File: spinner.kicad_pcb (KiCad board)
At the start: 2 copper layers, 39 parts, among them SW1 SW_SPDT, U1 SFH617A-3X006, U2 SFH617A-3X006, U3 SFH617A-3X006, U4 RS0102, U5 AP63205WU

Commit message: IDK.  Add the kitchen sink.
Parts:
- added C109: .1uF, Capacitor_SMD:C_0805_2012Metric_Pad1.18x1.45mm_HandSolder, B.Cu at (145.0, 154.0)
- added C110: .1uF, Capacitor_SMD:C_0805_2012Metric_Pad1.18x1.45mm_HandSolder, B.Cu at (145.0, 160.0)
- added C111: .1uF, Capacitor_SMD:C_0805_2012Metric_Pad1.18x1.45mm_HandSolder, B.Cu at (145.0, 166.0)
- added C112: .1uF, Capacitor_SMD:C_0805_2012Metric_Pad1.18x1.45mm_HandSolder, B.Cu at (145.0, 172.0)
- added C113: .1uF, Capacitor_SMD:C_0805_2012Metric_Pad1.18x1.45mm_HandSolder, B.Cu at (145.0, 178.0)
- added C114: .1uF, Capacitor_SMD:C_0805_2012Metric_Pad1.18x1.45mm_HandSolder, B.Cu at (145.0, 184.0)
- added C115: .1uF, Capacitor_SMD:C_0805_2012Metric_Pad1.18x1.45mm_HandSolder, B.Cu at (145.0, 190.0)
- added C201: .1uF, Capacitor_SMD:C_0805_2012Metric_Pad1.18x1.45mm_HandSolder, B.Cu at (157.7, 101.3)
- added C202: .1uF, Capacitor_SMD:C_0805_2012Metric_Pad1.18x1.45mm_HandSolder, B.Cu at (162.9, 98.3)
- added C203: .1uF, Capacitor_SMD:C_0805_2012Metric_Pad1.18x1.45mm_HandSolder, B.Cu at (168.1, 95.3)
- added C204: .1uF, Capacitor_SMD:C_0805_2012Metric_Pad1.18x1.45mm_HandSolder, B.Cu at (173.3, 92.3)
- added C205: .1uF, Capacitor_SMD:C_0805_2012Metric_Pad1.18x1.45mm_HandSolder, B.Cu at (178.5, 89.3)
- added C206: .1uF, Capacitor_SMD:C_0805_2012Metric_Pad1.18x1.45mm_HandSolder, B.Cu at (183.7, 86.3)
- added C207: .1uF, Capacitor_SMD:C_0805_2012Metric_Pad1.18x1.45mm_HandSolder, B.Cu at (188.9, 83.3)
- added C208: .1uF, Capacitor_SMD:C_0805_2012Metric_Pad1.18x1.45mm_HandSolder, B.Cu at (194.1, 80.3)
- added C209: .1uF, Capacitor_SMD:C_0805_2012Metric_Pad1.18x1.45mm_HandSolder, B.Cu at (199.3, 77.3)
- added C210: .1uF, Capacitor_SMD:C_0805_2012Metric_Pad1.18x1.45mm_HandSolder, B.Cu at (204.5, 74.3)
- added C211: .1uF, Capacitor_SMD:C_0805_2012Metric_Pad1.18x1.45mm_HandSolder, B.Cu at (209.7, 71.3)
- added C212: .1uF, Capacitor_SMD:C_0805_2012Metric_Pad1.18x1.45mm_HandSolder, B.Cu at (214.9, 68.3)
- added C213: .1uF, Capacitor_SMD:C_0805_2012Metric_Pad1.18x1.45mm_HandSolder, B.Cu at (220.0, 65.3)
- added C214: .1uF, Capacitor_SMD:C_0805_2012Metric_Pad1.18x1.45mm_HandSolder, B.Cu at (225.2, 62.3)
- added C215: .1uF, Capacitor_SMD:C_0805_2012Metric_Pad1.18x1.45mm_HandSolder, B.Cu at (230.4, 59.3)
- added C301: .1uF, Capacitor_SMD:C_0805_2012Metric_Pad1.18x1.45mm_HandSolder, B.Cu at (147.3, 92.7)
- added C302: .1uF, Capacitor_SMD:C_0805_2012Metric_Pad1.18x1.45mm_HandSolder, B.Cu at (142.1, 89.7)
- added C303: .1uF, Capacitor_SMD:C_0805_2012Metric_Pad1.18x1.45mm_HandSolder, B.Cu at (136.9, 86.7)
- added C304: .1uF, Capacitor_SMD:C_0805_2012Metric_Pad1.18x1.45mm_HandSolder, B.Cu at (131.7, 83.7)
- added C305: .1uF, Capacitor_SMD:C_0805_2012Metric_Pad1.18x1.45mm_HandSolder, B.Cu at (126.5, 80.7)
- added C306: .1uF, Capacitor_SMD:C_0805_2012Metric_Pad1.18x1.45mm_HandSolder, B.Cu at (121.3, 77.7)
- added C307: .1uF, Capacitor_SMD:C_0805_2012Metric_Pad1.18x1.45mm_HandSolder, B.Cu at (116.1, 74.7)
- added C308: .1uF, Capacitor_SMD:C_0805_2012Metric_Pad1.18x1.45mm_HandSolder, B.Cu at (110.9, 71.7)
- added C309: .1uF, Capacitor_SMD:C_0805_2012Metric_Pad1.18x1.45mm_HandSolder, B.Cu at (105.7, 68.7)
- added C310: .1uF, Capacitor_SMD:C_0805_2012Metric_Pad1.18x1.45mm_HandSolder, B.Cu at (100.5, 65.7)
- added C311: .1uF, Capacitor_SMD:C_0805_2012Metric_Pad1.18x1.45mm_HandSolder, B.Cu at (95.3, 62.7)
- added C312: .1uF, Capacitor_SMD:C_0805_2012Metric_Pad1.18x1.45mm_HandSolder, B.Cu at (90.1, 59.7)
- added C313: .1uF, Capacitor_SMD:C_0805_2012Metric_Pad1.18x1.45mm_HandSolder, B.Cu at (85.0, 56.7)
- added C314: .1uF, Capacitor_SMD:C_0805_2012Metric_Pad1.18x1.45mm_HandSolder, B.Cu at (79.8, 53.7)
- added C315: .1uF, Capacitor_SMD:C_0805_2012Metric_Pad1.18x1.45mm_HandSolder, B.Cu at (74.6, 50.7)
- added D109: APA102, LED_SMD:LED_RGB_5050-6, B.Cu at (150.0, 154.0)
- added D110: APA102, LED_SMD:LED_RGB_5050-6, B.Cu at (150.0, 160.0)
- added D111: APA102, LED_SMD:LED_RGB_5050-6, B.Cu at (150.0, 166.0)
- added D112: APA102, LED_SMD:LED_RGB_5050-6, B.Cu at (150.0, 172.0)
- added D113: APA102, LED_SMD:LED_RGB_5050-6, B.Cu at (150.0, 178.0)
- added D114: APA102, LED_SMD:LED_RGB_5050-6, B.Cu at (150.0, 184.0)
- added D115: APA102, LED_SMD:LED_RGB_5050-6, B.Cu at (150.0, 190.0)
- added D201: APA102, LED_SMD:LED_RGB_5050-6, B.Cu at (155.2, 97.0)
- added D202: APA102, LED_SMD:LED_RGB_5050-6, B.Cu at (160.4, 94.0)
- added D203: APA102, LED_SMD:LED_RGB_5050-6, B.Cu at (165.6, 91.0)
- added D204: APA102, LED_SMD:LED_RGB_5050-6, B.Cu at (170.8, 88.0)
- added D205: APA102, LED_SMD:LED_RGB_5050-6, B.Cu at (176.0, 85.0)
- added D206: APA102, LED_SMD:LED_RGB_5050-6, B.Cu at (181.2, 82.0)
- added D207: APA102, LED_SMD:LED_RGB_5050-6, B.Cu at (186.4, 79.0)
- added D208: APA102, LED_SMD:LED_RGB_5050-6, B.Cu at (191.6, 76.0)
- added D209: APA102, LED_SMD:LED_RGB_5050-6, B.Cu at (196.8, 73.0)
- added D210: APA102, LED_SMD:LED_RGB_5050-6, B.Cu at (202.0, 70.0)
- added D211: APA102, LED_SMD:LED_RGB_5050-6, B.Cu at (207.2, 67.0)
- added D212: APA102, LED_SMD:LED_RGB_5050-6, B.Cu at (212.4, 64.0)
- added D213: APA102, LED_SMD:LED_RGB_5050-6, B.Cu at (217.5, 61.0)
- added D214: APA102, LED_SMD:LED_RGB_5050-6, B.Cu at (222.7, 58.0)
- added D215: APA102, LED_SMD:LED_RGB_5050-6, B.Cu at (227.9, 55.0)
- added D301: APA102, LED_SMD:LED_RGB_5050-6, B.Cu at (144.8, 97.0)
- added D302: APA102, LED_SMD:LED_RGB_5050-6, B.Cu at (139.6, 94.0)
- added D303: APA102, LED_SMD:LED_RGB_5050-6, B.Cu at (134.4, 91.0)
- added D304: APA102, LED_SMD:LED_RGB_5050-6, B.Cu at (129.2, 88.0)
- added D305: APA102, LED_SMD:LED_RGB_5050-6, B.Cu at (124.0, 85.0)
- added D306: APA102, LED_SMD:LED_RGB_5050-6, B.Cu at (118.8, 82.0)
- added D307: APA102, LED_SMD:LED_RGB_5050-6, B.Cu at (113.6, 79.0)
- added D308: APA102, LED_SMD:LED_RGB_5050-6, B.Cu at (108.4, 76.0)
- added D309: APA102, LED_SMD:LED_RGB_5050-6, B.Cu at (103.2, 73.0)
- added D310: APA102, LED_SMD:LED_RGB_5050-6, B.Cu at (98.0, 70.0)
- added D311: APA102, LED_SMD:LED_RGB_5050-6, B.Cu at (92.8, 67.0)
- added D312: APA102, LED_SMD:LED_RGB_5050-6, B.Cu at (87.6, 64.0)
- added D313: APA102, LED_SMD:LED_RGB_5050-6, B.Cu at (82.5, 61.0)
- added D314: APA102, LED_SMD:LED_RGB_5050-6, B.Cu at (77.3, 58.0)
- added D315: APA102, LED_SMD:LED_RGB_5050-6, B.Cu at (72.1, 55.0)
- BT1, BT2, BT3, BT4, BT5, BT6: footprint Battery:BatteryHolder_Keystone_2460_1xAA -> Library:Spinner_BatteryHolder_Keystone_2460_1xAA
- C101: renamed from C5; moved to B.Cu
- C102: renamed from C6; moved to B.Cu
- C103: renamed from C7; moved to B.Cu
- C104: renamed from C8; moved to B.Cu
- C105: renamed from C9; moved to B.Cu
- C106: renamed from C10; moved to B.Cu
- C107: renamed from C11; moved to B.Cu
- C108: renamed from C12; moved to B.Cu
- D101: renamed from D1; moved to B.Cu
- D102: renamed from D2; moved to B.Cu
- D103: renamed from D3; moved to B.Cu
- D104: renamed from D4; moved to B.Cu
- D105: renamed from D5; moved to B.Cu
- D106: renamed from D6; moved to B.Cu
- D107: renamed from D7; moved to B.Cu
- D108: renamed from D8; moved to B.Cu
- moved I2 280.7 mm to (75.0, 105.0), turned to 180 degrees
- moved R2 279.1 mm to (74.0, 93.0), turned to 180 degrees
- moved U5 276.0 mm to (119.0, 105.0)
- moved U2 273.9 mm to (70.0, 98.6), turned to -1 degrees
- moved C4 256.3 mm to (117.0, 99.0)
- moved C2 242.4 mm to (121.0, 102.0), turned to 180 degrees
- moved C103 240.9 mm to (145.0, 118.0), turned to 90 degrees
- moved D101 240.5 mm to (150.0, 106.0), turned to 180 degrees
- moved C1 238.9 mm to (119.0, 108.0)
- moved C102 236.6 mm to (145.0, 112.0), turned to 90 degrees
- moved SW1 236.3 mm to (109.0, 35.0), turned to -150 degrees
- moved D107 233.8 mm to (150.0, 142.0), turned to 180 degrees
- moved D108 232.9 mm to (150.0, 148.0), turned to 180 degrees
- moved C108 231.3 mm to (145.0, 148.0), turned to 90 degrees
- moved D104 225.1 mm to (150.0, 124.0), turned to 180 degrees
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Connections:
- A1 pad 10: unconnected-(A1-Pad10) -> /OPTO_in_2
- A1 pad 11: unconnected-(A1-Pad11) -> /GPIO_14
- A1 pad 13: +3V3 -> /GPIO_13
- A1 pad 14: unconnected-(A1-Pad14) -> +3V3
- A1 pad 15: unconnected-(A1-Pad15) -> GND
- A1 pad 16: unconnected-(A1-Pad16) -> VCC
- A1 pad 17: unconnected-(A1-Pad17) -> (no net)
- A1 pad 18: unconnected-(A1-Pad18) -> (no net)
- A1 pad 19: unconnected-(A1-Pad19) -> (no net)
- A1 pad 2: unconnected-(A1-Pad2) -> (no net)
- A1 pad 20: unconnected-(A1-Pad20) -> (no net)
- A1 pad 3: unconnected-(A1-Pad3) -> (no net)
- A1 pad 4: unconnected-(A1-Pad4) -> (no net)
- A1 pad 5: unconnected-(A1-Pad5) -> (no net)
- A1 pad 6: unconnected-(A1-Pad6) -> (no net)
- A1 pad 7: unconnected-(A1-Pad7) -> (no net)
- A1 pad 8: VCC -> /OPTO_in_0
- A1 pad 9: unconnected-(A1-Pad9) -> /OPTO_in_1
- D108 pad 5: unconnected-(D8-Pad5) -> Net-(D108-Pad5)
- D108 pad 6: unconnected-(D8-Pad6) -> Net-(D108-Pad6)
- SW1 pad 1: Net-(C1-Pad1) -> unconnected-(SW1-Pad1)
- SW1 pad 3: unconnected-(SW1-Pad3) -> Net-(C1-Pad1)
- U1 pad 2: GND -> Net-(U1-Pad2)
- U2 pad 2: Net-(U2-Pad2) -> GND
- U3 pad 1: Net-(U2-Pad2) -> Net-(U1-Pad2)

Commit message: Update things.  Next checkin.
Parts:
- added H101: MountingHole, MountingHole:MountingHole_3mm, F.Cu at (116.7, 89.2)
- added H102: MountingHole, MountingHole:MountingHole_3mm, F.Cu at (157.3, 134.2)
- added H103: MountingHole, MountingHole:MountingHole_3mm, F.Cu at (135.3, 108.5)
- added H104: MountingHole, MountingHole:MountingHole_3mm, F.Cu at (184.0, 91.5)
- added H105: MountingHole, MountingHole:MountingHole_3mm, F.Cu at (140.4, 133.6)
- added H106: MountingHole, MountingHole:MountingHole_3mm, F.Cu at (176.0, 76.6)
- added H107: MountingHole, MountingHole:MountingHole_3mm, F.Cu at (164.7, 108.5)
- added H108: MountingHole, MountingHole:MountingHole_3mm, F.Cu at (125.7, 74.8)
- added H109: MountingHole, MountingHole:MountingHole_3mm, F.Cu at (150.0, 83.0)
- moved U104 16.6 mm to (162.6, 78.7)
- moved A101 5.42 mm to (149.9, 63.5)
- renumbered A1 to A101, BT1 to BT101, BT2 to BT102, BT3 to BT103, BT4 to BT104, BT5 to BT105, BT6 to BT106, C1 to C101, C2 to C102, C3 to C103, C4 to C104, C301 to C105, C101 to C106, C201 to C107, C302 to C108, C102 to C109, C202 to C110, C303 to C111, C103 to C112, C203 to C113, C304 to C114, C104 to C115, C204 to C116, C305 to C117, C105 to C118, C205 to C119, C306 to C120, C106 to C121, C206 to C122, C307 to C123, C107 to C124, C207 to C125, C308 to C126, C108 to C127, C208 to C128, C309 to C129, C109 to C130, C209 to C131, C310 to C132, C110 to C133, C210 to C134, C311 to C135, C111 to C136, C211 to C137, C312 to C138, C112 to C139, C212 to C140, C313 to C141, C113 to C142, C213 to C143, C314 to C144, C114 to C145, C214 to C146, C315 to C147, C115 to C148, C215 to C149, D301 to D101, D101 to D102, D201 to D103, D302 to D104, D102 to D105, D202 to D106, D303 to D107, D103 to D108, D203 to D109, D304 to D110, D104 to D111, D204 to D112, D305 to D113, D105 to D114, D205 to D115, D306 to D116, D106 to D117, D206 to D118, D307 to D119, D107 to D120, D207 to D121, D308 to D122, D108 to D123, D208 to D124, D309 to D125, D109 to D126, D209 to D127, D310 to D128, D110 to D129, D210 to D130, D311 to D131, D111 to D132, D211 to D133, D312 to D134, D112 to D135, D212 to D136, D313 to D137, D113 to D138, D213 to D139, D314 to D140, D114 to D141, D214 to D142, D315 to D143, D115 to D144, D215 to D145, I1 to I101, I2 to I102, L1 to L101, R1 to R101, R2 to R102, R3 to R103, SW1 to SW101, U1 to U101, U2 to U102, U3 to U103, U4 to U104, U5 to U105
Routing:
- net VCC: track 0.00 -> 254.6 mm, vias 0 -> 45
- net /OPTO_in_1: track 0.00 -> 116.5 mm
- net /CO_3: track 0.00 -> 114.3 mm, vias 0 -> 2
- net /OPTO_in_0: track 0.00 -> 109.8 mm
- net /CO_1: track 0.00 -> 104.7 mm
- net /DO_3: track 0.00 -> 101.9 mm, vias 0 -> 2
- net /DO_1: track 0.00 -> 99.6 mm
- net Net-(C101-Pad1): track 0.00 -> 74.3 mm
- net /OPTO_in_2: track 0.00 -> 70.9 mm
- net /CI: track 0.00 -> 52.9 mm, vias 0 -> 1
- net Net-(U101-Pad2): track 0.00 -> 48.7 mm
- net /DI: track 0.00 -> 47.7 mm, vias 0 -> 1
- net GND: track 0.00 -> 31.2 mm, vias 0 -> 6
- net Net-(BT101-Pad2): track 0.00 -> 18.1 mm
- net Net-(BT104-Pad2): track 0.00 -> 16.0 mm
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- added copper zone on B.Cu, net GND
- added copper zone on F.Cu, net VCC
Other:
- board outline added: 190 x 190 mm

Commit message: Adding all kinds of things.
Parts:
- added G***: LOGO, Library:hakz_04, B.Cu at (152.5, 34.0)
- moved BT101 0.96 mm to (150.0, 39.0)

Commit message: Updated schematic and things.  For spin 2.  And board layout.
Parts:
- added TP1: GND, TestPoint:TestPoint_Pad_D2.5mm, F.Cu at (95.4, 28.9)
- added TP2: 3v3, TestPoint:TestPoint_Pad_D2.5mm, F.Cu at (132.2, 13.0)
- added TP3: Opto_1, TestPoint:TestPoint_Pad_D2.5mm, F.Cu at (188.7, 20.0)
- added TP4: VCC, TestPoint:TestPoint_Pad_D2.5mm, F.Cu at (118.2, 16.2)
- added TP5: BATT, TestPoint:TestPoint_Pad_D2.5mm, F.Cu at (106.2, 21.9)
- added TP6: Opto_0, TestPoint:TestPoint_Pad_D2.5mm, F.Cu at (174.8, 14.9)
- added TP7: DI, TestPoint:TestPoint_Pad_D2.5mm, F.Cu at (158.9, 11.1)
- added TP8: CI, TestPoint:TestPoint_Pad_D2.5mm, F.Cu at (146.8, 11.1)
- added TP9: Opto_2, TestPoint:TestPoint_Pad_D2.5mm, F.Cu at (200.2, 26.3)
- C102: value 100nF -> .1uF
- moved R103 11.3 mm to (199.5, 101.9), turned to 90 degrees
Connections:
- R101 pad 1: VCC -> +3V3
- R102 pad 1: VCC -> +3V3
- R103 pad 1: VCC -> +3V3
- U101 pad 3: GND -> /OPTO_in_0
- U101 pad 4: /OPTO_in_0 -> GND
- U102 pad 3: GND -> /OPTO_in_1
- U102 pad 4: /OPTO_in_1 -> GND
- U103 pad 3: GND -> /OPTO_in_2
- U103 pad 4: /OPTO_in_2 -> GND
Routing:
- net +3V3: track 8.04 -> 330.3 mm, vias 0 -> 3
- net /OPTO_in_1: track 116.5 -> 218.3 mm, vias 0 -> 1
- net /CI: track 52.9 -> 147.4 mm, vias 1 -> 3
- net /OPTO_in_2: track 70.9 -> 156.2 mm, vias 0 -> 1
- net /DI: track 47.7 -> 128.0 mm, vias 1 -> 5
- net /OPTO_in_0: track 109.8 -> 174.7 mm
- net +BATT: track 14.6 -> 31.9 mm
- net GND: track 31.2 -> 34.5 mm, vias 6 -> 7
- net Net-(U101-Pad2): track 48.7 -> 49.7 mm
- net /GPIO_14: track 6.91 -> 6.33 mm

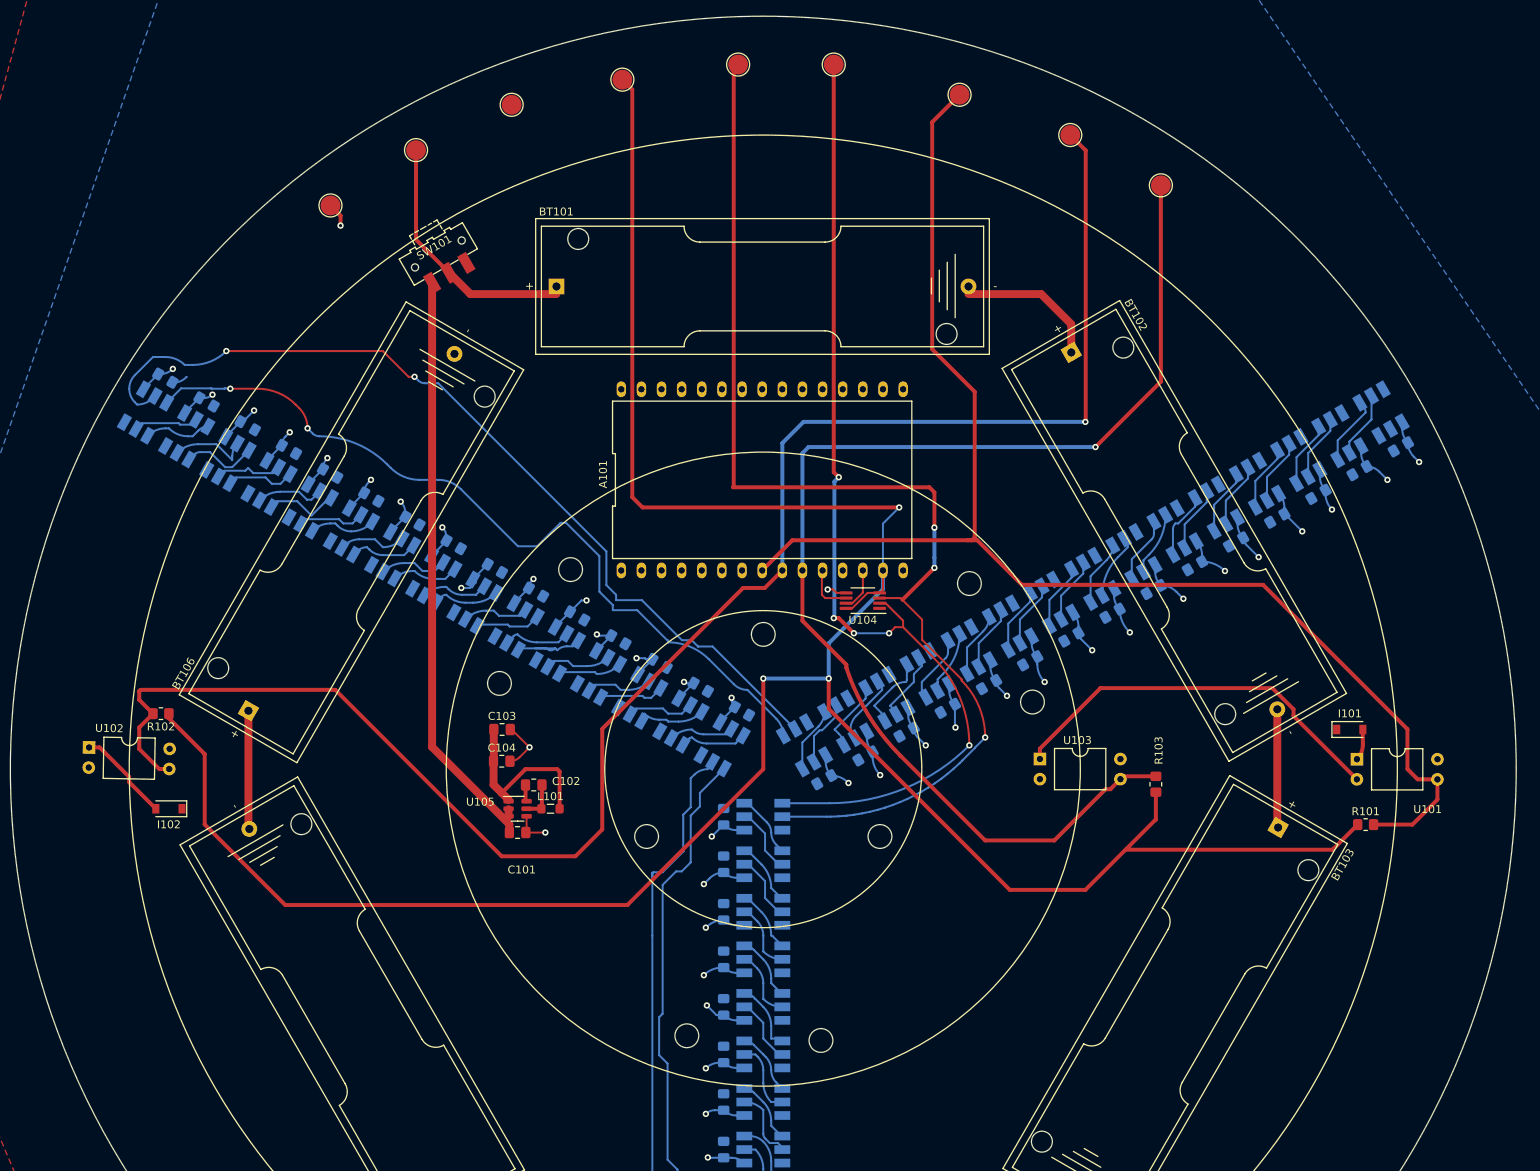
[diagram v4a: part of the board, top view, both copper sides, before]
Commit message: Adding things: SD card, resistor pack, routing.  Totally done.
Issue: HKZ-563
Changelog: No Functional Change.
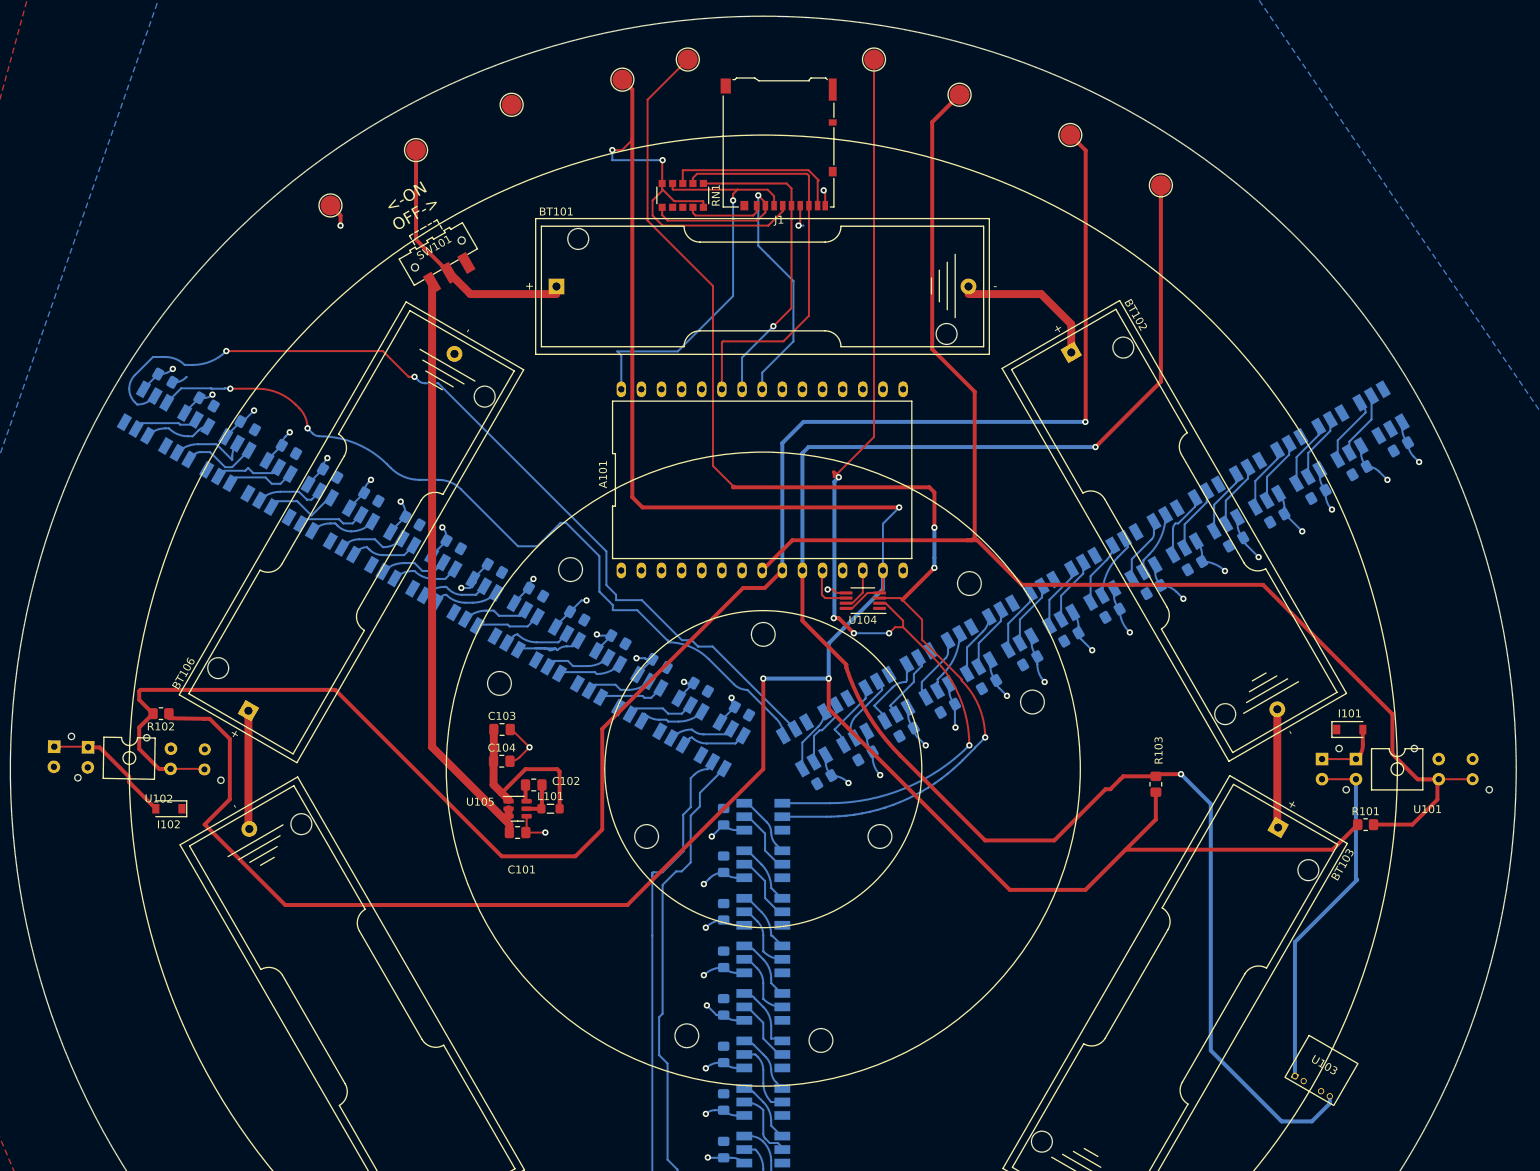
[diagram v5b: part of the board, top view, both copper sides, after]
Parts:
- added J1: Micro_SD_Card, Connector_Card:microSD_HC_Hirose_DM3AT-SF-PEJM5, F.Cu at (151.9, 21.2)
- added RN1: R_Network08, Resistor_SMD:R_Array_Convex_5x1206, F.Cu at (139.8, 27.6)
- U101, U102: footprint Package_DIP:DIP-4_W10.16mm -> Library:MULTI_PART_THRU_BEAM
- U103: footprint Package_DIP:DIP-4_W10.16mm -> Library:tcrt1000
- moved U103 49.6 mm to (219.3, 140.0), turned to -30 degrees
- moved TP8 6.38 mm to (140.5, 10.5)
- moved TP7 5.12 mm to (164.0, 10.5)
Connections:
- A101 pad 23: (no net) -> /spi_cs
- A101 pad 24: (no net) -> /spi_clk
- A101 pad 25: (no net) -> /spi_in
- A101 pad 30: (no net) -> /spi_out
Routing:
- net /OPTO_in_2: track 156.2 -> 216.5 mm, vias 1 -> 2
- net /spi_in: track 0.00 -> 51.6 mm
- net /spi_out: track 0.00 -> 51.2 mm, vias 0 -> 1
- net +3V3: track 330.3 -> 378.4 mm, vias 3 -> 5
- net /spi_cs: track 0.00 -> 45.2 mm, vias 0 -> 1
- net /spi_clk: track 0.00 -> 39.3 mm, vias 0 -> 1
- net Net-(J1-Pad8): track 0.00 -> 22.6 mm
- net Net-(J1-Pad1): track 0.00 -> 9.87 mm
- net /CI: track 147.4 -> 154.4 mm
- net GND: track 34.5 -> 39.7 mm, vias 7 -> 9
- net Net-(U101-Pad2): track 49.7 -> 45.0 mm
- net /OPTO_in_1: track 218.3 -> 222.6 mm
- net Net-(I102-Pad2): track 12.0 -> 16.3 mm
- net Net-(I101-Pad2): track 3.94 -> 8.21 mm
- net /OPTO_in_0: track 174.7 -> 179.0 mm
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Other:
- board text added: "<-ON OFF->"
